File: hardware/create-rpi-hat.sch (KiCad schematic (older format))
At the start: 22 parts, among them IC1 LMZ21701SILT, J1 Roomba_conn, J2 USB_B_Micro, J3 RaspberryPi GPIO connector, U2 TXS0102DCT, U3 FT230XS, U4 NUP2202

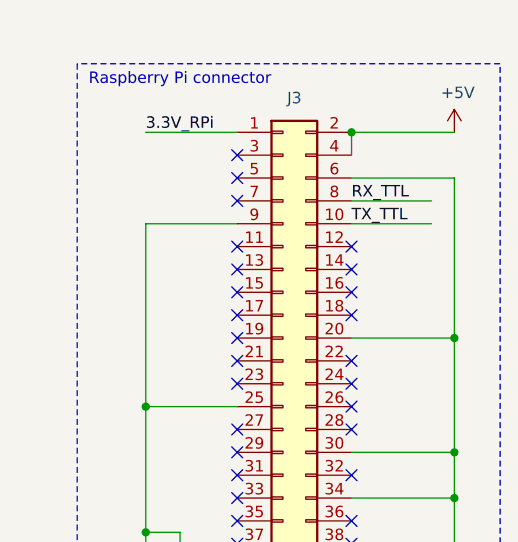
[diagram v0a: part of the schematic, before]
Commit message: Removed power pours and made more space for the buck module
The latter is against module's layout recommendations, but makes
soldering/rework easier
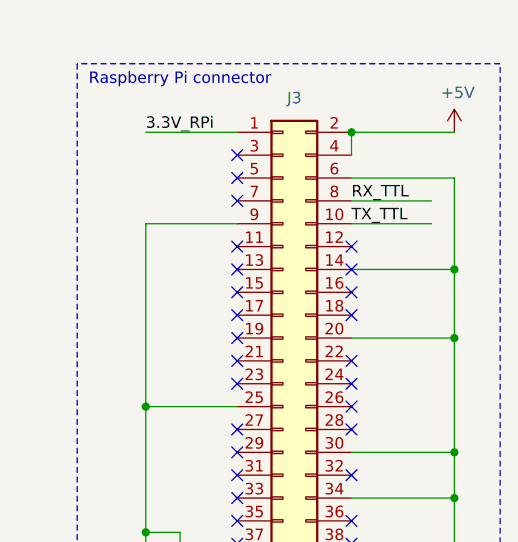
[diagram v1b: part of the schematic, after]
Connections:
- wire segments 113 -> 115
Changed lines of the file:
@@
 	3500 5500 4000 5500
 Wire Wire Line
-	10250 1650 10250 2350
+	10250 1650 10250 2050
 NoConn ~ 9800 2050
 $Comp
@@
 Text Notes 7150 3750 0    50   ~ 0
 Mixing 3.3V sources
+Wire Wire Line
+	9800 2050 10250 2050
+Connection ~ 10250 2050
+Wire Wire Line
+	10250 2050 10250 2350
 $EndSCHEMATC

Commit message: Revision 0.9 (also ordered on Aisler)
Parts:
- removed J1: Roomba_conn, kicad-libs:CUI_TB001-500-05BE, symbol Connector_Generic:Conn_01x05
- added C7: 100n, Capacitor_SMD:C_0402_1005Metric, symbol Device:C_Small
- added C8: 4.7u, Capacitor_SMD:C_0402_1005Metric, symbol Device:C_Small
- added J1: Mini-DIN-8, kicad-libs:CUI_MD-80SM, symbol Connector:Mini-DIN-8
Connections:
- wire segments 115 -> 118
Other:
- moved on the sheet: C2
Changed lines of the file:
@@
 Wire Wire Line
 	10150 1750 9800 1750
-Text Label 1500 4800 0    50   ~ 0
+Text Label 2150 5300 0    50   ~ 0
 VIN_Roomba
 $Comp
@@
 	1    0    0    -1
 $EndComp
-Wire Wire Line
-	2800 2300 2900 2300
 Wire Wire Line
 	3050 2300 3050 2350
@@
 	1    0    0    -1
 $EndComp
-Text Label 1200 5100 0    50   ~ 0
+Text Label 2150 5200 0    50   ~ 0
 RX_Roomba
-Text Label 1200 5000 0    50   ~ 0
+Text Label 1100 5200 0    50   ~ 0
 TX_Roomba
 Wire Notes Line style solid
@@
 Text Label 3050 2000 0    50   ~ 0
 VIN_Roomba
-$Comp
-L power:+5V #PWR07
-U 1 1 5E7AFE4A
-P 3500 5900
-F 0 "#PWR07" H 3500 5750 50  0001 C CNN
-F 1 "+5V" H 3515 6073 50  0000 C CNN
-F 2 "" H 3500 5900 50  0001 C CNN
-F 3 "" H 3500 5900 50  0001 C CNN
-	1    3500 5900
-	1    0    0    -1
-$EndComp
 Wire Notes Line style solid
 	3350 4700 5850 4700
@@
 	6500 1800 6750 1800
 Text Label 6550 1800 0    50   ~ 0
+TX_TTL
+Text Label 6550 1900 0    50   ~ 0
 RX_TTL
-Text Label 6550 1900 0    50   ~ 0
-TX_TTL
 Text Label 4750 2100 0    50   ~ 0
 USBDM
@@
 L power:GND #PWR02
 U 1 1 5E53BB99
-P 1550 5350
-F 0 "#PWR02" H 1550 5100 50  0001 C CNN
-F 1 "GND" H 1555 5177 50  0000 C CNN
-F 2 "" H 1550 5350 50  0001 C CNN
-F 3 "" H 1550 5350 50  0001 C CNN
-	1    1550 5350
+P 1350 4900
+F 0 "#PWR02" H 1350 4650 50  0001 C CNN
+F 1 "GND" H 1355 4727 50  0000 C CNN
+F 2 "" H 1350 4900 50  0001 C CNN
+F 3 "" H 1350 4900 50  0001 C CNN
+	1    1350 4900
 	1    0    0    -1
 $EndComp
@@
 L power:PWR_FLAG #FLG0101
 U 1 1 5EE2593F
-P 1650 4900
-F 0 "#FLG0101" H 1650 4975 50  0001 C CNN
-F 1 "PWR_FLAG" H 1650 5073 50  0001 C CNN
-F 2 "" H 1650 4900 50  0001 C CNN
-F 3 "~" H 1650 4900 50  0001 C CNN
-	1    1650 4900
-	1    0    0    -1
-$EndComp
-$Comp
-L Connector_Generic:Conn_01x05 J1
-U 1 1 5EC8659D
-P 1900 5100
-F 0 "J1" H 1980 5142 50  0000 L CNN
-F 1 "Roomba_conn" H 1980 5051 50  0000 L CNN
-F 2 "kicad-libs:CUI_TB001-500-05BE" H 1900 5100 50  0001 C CNN
-F 3 "~" H 1900 5100 50  0001 C CNN
-	1    1900 5100
-	1    0    0    -1
-$EndComp
-Wire Wire Line
-	1700 5300 1550 5300
-Wire Wire Line
-	1550 5300 1550 5350
-Wire Wire Line
-	1700 4900 1650 4900
-Wire Wire Line
-	1500 4900 1500 4800
-Wire Wire Line
-	1700 5100 1200 5100
-Wire Wire Line
-	1700 5000 1200 5000
-NoConn ~ 1700 5200
+P 1050 5300
+F 0 "#FLG0101" H 1050 5375 50  0001 C CNN
+F 1 "PWR_FLAG" H 1050 5473 50  0001 C CNN
+F 2 "" H 1050 5300 50  0001 C CNN
+F 3 "~" H 1050 5300 50  0001 C CNN
+	1    1050 5300
+	1    0    0    -1
+$EndComp
 Wire Notes Line style solid
 	1000 4350 1000 5900
-Connection ~ 1650 4900
-Wire Wire Line
-	1650 4900 1500 4900
 Wire Notes Line style solid
 	2700 5900 1000 5900
@@
 L power:+5V #PWR09
 U 1 1 5E5D9AFB
+P 4500 4950
+F 0 "#PWR09" H 4500 4800 50  0001 C CNN
+F 1 "+5V" H 4515 5123 50  0000 C CNN
+F 2 "" H 4500 4950 50  0001 C CNN
+F 3 "" H 4500 4950 50  0001 C CNN
+	1    4500 4950
+	1    0    0    -1
+$EndComp
+Wire Wire Line
+	4300 4950 4300 5000
+$Comp
+L power:+3.3V #PWR010
+U 1 1 5E5E106D
 P 4300 4950
-F 0 "#PWR09" H 4300 4800 50  0001 C CNN
-F 1 "+5V" H 4315 5123 50  0000 C CNN
+F 0 "#PWR010" H 4300 4800 50  0001 C CNN
+F 1 "+3.3V" H 4315 5123 50  0000 C CNN
 F 2 "" H 4300 4950 50  0001 C CNN
 F 3 "" H 4300 4950 50  0001 C CNN
 	1    4300 4950
-	1    0    0    -1
-$EndComp
-Wire Wire Line
-	4300 4950 4300 5000
-$Comp
-L power:+3.3V #PWR010
-U 1 1 5E5E106D
-P 4500 4950
-F 0 "#PWR010" H 4500 4800 50  0001 C CNN
-F 1 "+3.3V" H 4515 5123 50  0000 C CNN
-F 2 "" H 4500 4950 50  0001 C CNN
-F 3 "" H 4500 4950 50  0001 C CNN
-	1    4500 4950
 	1    0    0    -1
 $EndComp
@@
 $EndComp
 Text Label 5050 5700 0    50   ~ 0
-TX_TTL
+TX_Roomba
 Text Label 5050 5500 0    50   ~ 0
-RX_TTL
+RX_Roomba
 Wire Wire Line
 	4800 5700 5250 5700
@@
 	4000 5900 3500 5900
 Text Label 3500 5700 0    50   ~ 0
-TX_Roomba
+TX_TTL
 Wire Wire Line
 	4000 5700 3500 5700
 Text Label 3500 5500 0    50   ~ 0
-RX_Roomba
+RX_TTL
 Wire Wire Line
 	4400 6100 4950 6100
@@
 Wire Wire Line
 	10250 1650 10250 2050
-NoConn ~ 9800 2050
 $Comp
 L LMZ21701SILT:LMZ21701SILT IC1
@@
 	2800 2000 2800 2100
 Connection ~ 2800 2000
-Wire Wire Line
-	2800 2000 2900 2000
 $Comp
 L Device:C_Small C2
 U 1 1 5E5CB833
-P 2900 2100
-F 0 "C2" H 2992 2146 50  0000 L CNN
-F 1 "22u" H 2992 2055 50  0000 L CNN
-F 2 "Capacitor_SMD:C_0805_2012Metric_Pad1.15x1.40mm_HandSolder" H 2900 2100 50  0001 C CNN
-F 3 "~" H 2900 2100 50  0001 C CNN
-	1    2900 2100
-	1    0    0    -1
-$EndComp
-Connection ~ 2900 2000
-Wire Wire Line
-	2900 2000 3050 2000
-Wire Wire Line
-	2900 2200 2900 2300
-Connection ~ 2900 2300
-Wire Wire Line
-	2900 2300 3050 2300
+P 2950 2150
+F 0 "C2" H 3042 2196 50  0000 L CNN
+F 1 "22u" H 3042 2105 50  0000 L CNN
+F 2 "Capacitor_SMD:C_0805_2012Metric_Pad1.15x1.40mm_HandSolder" H 2950 2150 50  0001 C CNN
+F 3 "~" H 2950 2150 50  0001 C CNN
+	1    2950 2150
+	1    0    0    -1
+$EndComp
 Wire Wire Line
 	1600 2100 1500 2100
@@
 Wire Wire Line
 	10250 2050 10250 2350
+$Comp
+L power:+3.3V #PWR0105
+U 1 1 5F0A6511
+P 3500 5900
+F 0 "#PWR0105" H 3500 5750 50  0001 C CNN
+F 1 "+3.3V" H 3500 6050 50  0000 C CNN
+F 2 "" H 3500 5900 50  0001 C CNN
+F 3 "" H 3500 5900 50  0001 C CNN
+	1    3500 5900
+	1    0    0    -1
+$EndComp
+$Comp
+L Connector:Mini-DIN-8 J1
+U 1 1 5F0B2F0D
+P 1850 5200
+F 0 "J1" H 1850 5681 50  0000 C CNN
+F 1 "Mini-DIN-8" H 1850 5590 50  0000 C CNN
+F 2 "kicad-libs:CUI_MD-80SM" V 1840 5190 50  0001 C CNN
+F 3 "https://www.cuidevices.com/product/resource/md-sm-series.pdf" V 1840 5190 50  0001 C CNN
+	1    1850 5200
+	1    0    0    -1
+$EndComp
+Text Label 1100 5300 0    50   ~ 0
+VIN_Roomba
+Wire Wire Line
+	1550 5200 1100 5200
+Wire Wire Line
+	1850 4900 1550 4900
+Wire Wire Line
+	1550 5100 1550 4900
+Connection ~ 1550 4900
+Wire Wire Line
+	1550 4900 1350 4900
+NoConn ~ 1850 5500
+NoConn ~ 2150 5100
+Wire Wire Line
+	1050 5300 1550 5300
+$Comp
+L Device:C_Small C7
+U 1 1 5F191542
+P 6650 1350
+F 0 "C7" H 6742 1396 50  0000 L CNN
+F 1 "100n" H 6742 1305 50  0000 L CNN
+F 2 "Capacitor_SMD:C_0402_1005Metric" H 6650 1350 50  0001 C CNN
+F 3 "~" H 6650 1350 50  0001 C CNN
+	1    6650 1350
+	1    0    0    -1
+$EndComp
+$Comp
+L Device:C_Small C8
+U 1 1 5F198622
+P 7050 1350
+F 0 "C8" H 7142 1396 50  0000 L CNN
+F 1 "4.7u" H 7142 1305 50  0000 L CNN
+F 2 "Capacitor_SMD:C_0402_1005Metric" H 7050 1350 50  0001 C CNN
+F 3 "~" H 7050 1350 50  0001 C CNN
+	1    7050 1350
+	1    0    0    -1
+$EndComp
+$Comp
+L power:GND #PWR0106
+U 1 1 5F1A7005
+P 6850 1450
+F 0 "#PWR0106" H 6850 1200 50  0001 C CNN
+F 1 "GND" H 6855 1277 50  0000 C CNN
+F 2 "" H 6850 1450 50  0001 C CNN
+F 3 "" H 6850 1450 50  0001 C CNN
+	1    6850 1450
+	1    0    0    -1
+$EndComp
+Wire Wire Line
+	6650 1450 6850 1450
+Wire Wire Line
+	7050 1450 6850 1450
+Connection ~ 6850 1450
+Wire Wire Line
+	7050 1250 6650 1250
+Wire Wire Line
+	6650 1250 6450 1250
+Connection ~ 6650 1250
+Text Label 6450 1250 0    50   ~ 0
+USBVBUS
+Wire Wire Line
+	2800 2000 2950 2000
+Wire Wire Line
+	2800 2300 2950 2300
+Wire Wire Line
+	2950 2250 2950 2300
+Connection ~ 2950 2300
+Wire Wire Line
+	2950 2300 3050 2300
+Wire Wire Line
+	2950 2050 2950 2000
+Connection ~ 2950 2000
+Wire Wire Line
+	2950 2000 3050 2000
 $EndSCHEMATC
